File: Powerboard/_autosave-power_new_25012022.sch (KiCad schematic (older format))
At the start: 14 parts

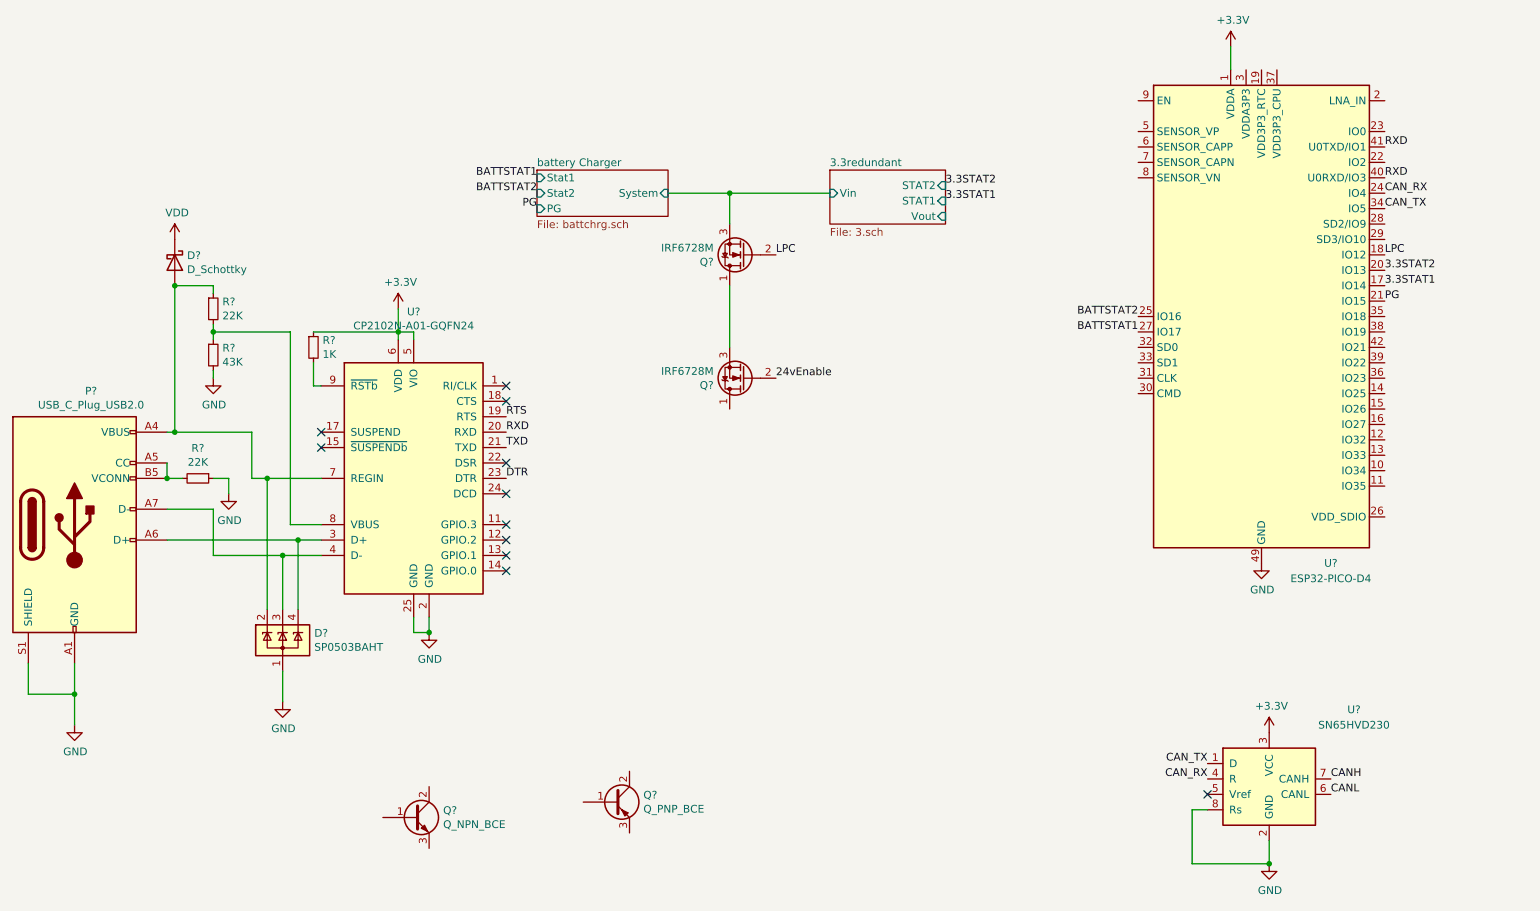
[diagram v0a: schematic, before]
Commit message: 13/02/2022
reverse polarity protection added, some test points, general clear up
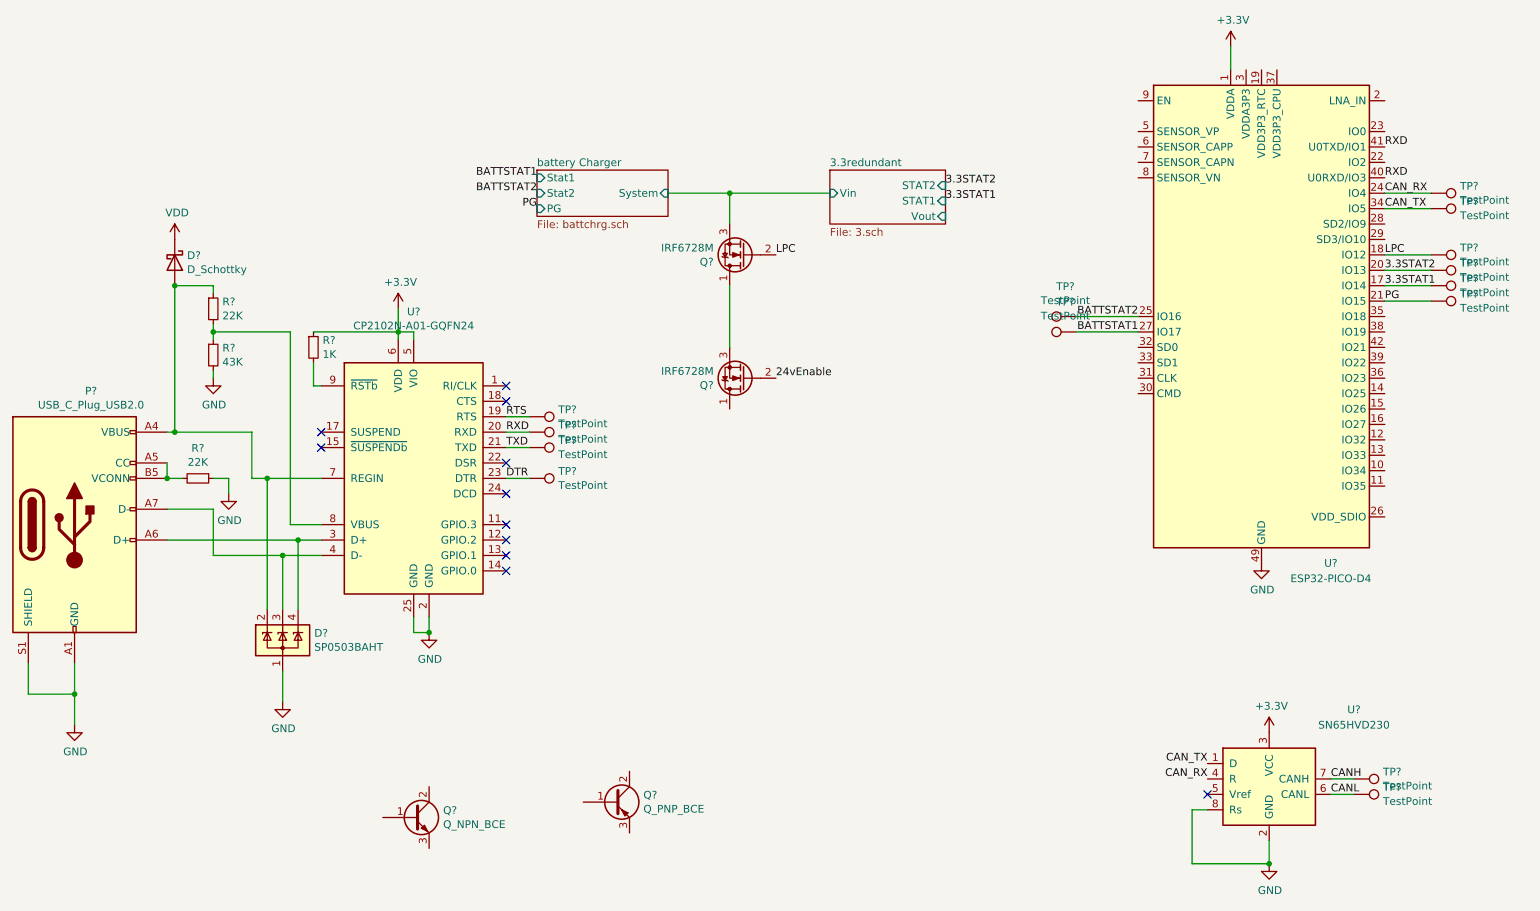
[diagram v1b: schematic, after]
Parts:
- added TP? (x14): TestPoint, symbol Connector:TestPoint
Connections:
- net 3.3STAT1: now also TP?.1
- net 3.3STAT2: now also TP?.1
- net BATTSTAT1: now also TP?.1
- net BATTSTAT2: now also TP?.1
- net CANH: now also TP?.1
- net CANL: now also TP?.1
- net CAN_RX: now also TP?.1
- net CAN_TX: now also TP?.1
- net DTR: now also TP?.1
- net LPC: now also TP?.1
- net PG: now also TP?.1
- net RTS: now also TP?.1
- net RXD: now also TP?.1
- net TXD: now also TP?.1
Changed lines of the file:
@@
 	1    0    0    -1
 $EndComp
+$Comp
+L Connector:TestPoint TP?
+U 1 1 620AFC71
+P 4700 3250
+F 0 "TP?" V 4654 3438 50  0000 L CNN
+F 1 "TestPoint" V 4745 3438 50  0000 L CNN
+F 2 "" H 4900 3250 50  0001 C CNN
+F 3 "~" H 4900 3250 50  0001 C CNN
+	1    4700 3250
+	0    1    1    0
+$EndComp
+$Comp
+L Connector:TestPoint TP?
+U 1 1 620B03B1
+P 4700 3350
+F 0 "TP?" V 4654 3538 50  0000 L CNN
+F 1 "TestPoint" V 4745 3538 50  0000 L CNN
+F 2 "" H 4900 3350 50  0001 C CNN
+F 3 "~" H 4900 3350 50  0001 C CNN
+	1    4700 3350
+	0    1    1    0
+$EndComp
+$Comp
+L Connector:TestPoint TP?
+U 1 1 620B05A4
+P 4700 3450
+F 0 "TP?" V 4654 3638 50  0000 L CNN
+F 1 "TestPoint" V 4745 3638 50  0000 L CNN
+F 2 "" H 4900 3450 50  0001 C CNN
+F 3 "~" H 4900 3450 50  0001 C CNN
+	1    4700 3450
+	0    1    1    0
+$EndComp
+$Comp
+L Connector:TestPoint TP?
+U 1 1 620B0755
+P 4700 3650
+F 0 "TP?" V 4654 3838 50  0000 L CNN
+F 1 "TestPoint" V 4745 3838 50  0000 L CNN
+F 2 "" H 4900 3650 50  0001 C CNN
+F 3 "~" H 4900 3650 50  0001 C CNN
+	1    4700 3650
+	0    1    1    0
+$EndComp
+Wire Wire Line
+	4550 3250 4700 3250
+Wire Wire Line
+	4700 3350 4550 3350
+Wire Wire Line
+	4700 3450 4550 3450
+Wire Wire Line
+	4700 3650 4550 3650
+$Comp
+L Connector:TestPoint TP?
+U 1 1 620B49A6
+P 10550 1800
+F 0 "TP?" V 10504 1988 50  0000 L CNN
+F 1 "TestPoint" V 10595 1988 50  0000 L CNN
+F 2 "" H 10750 1800 50  0001 C CNN
+F 3 "~" H 10750 1800 50  0001 C CNN
+	1    10550 1800
+	0    1    1    0
+$EndComp
+$Comp
+L Connector:TestPoint TP?
+U 1 1 620B4E68
+P 10550 1900
+F 0 "TP?" V 10504 2088 50  0000 L CNN
+F 1 "TestPoint" V 10595 2088 50  0000 L CNN
+F 2 "" H 10750 1900 50  0001 C CNN
+F 3 "~" H 10750 1900 50  0001 C CNN
+	1    10550 1900
+	0    1    1    0
+$EndComp
+Wire Wire Line
+	10550 1800 10250 1800
+Wire Wire Line
+	10550 1900 10250 1900
+$Comp
+L Connector:TestPoint TP?
+U 1 1 620B6EB6
+P 10550 2200
+F 0 "TP?" V 10504 2388 50  0000 L CNN
+F 1 "TestPoint" V 10595 2388 50  0000 L CNN
+F 2 "" H 10750 2200 50  0001 C CNN
+F 3 "~" H 10750 2200 50  0001 C CNN
+	1    10550 2200
+	0    1    1    0
+$EndComp
+$Comp
+L Connector:TestPoint TP?
+U 1 1 620B7211
+P 10550 2300
+F 0 "TP?" V 10504 2488 50  0000 L CNN
+F 1 "TestPoint" V 10595 2488 50  0000 L CNN
+F 2 "" H 10750 2300 50  0001 C CNN
+F 3 "~" H 10750 2300 50  0001 C CNN
+	1    10550 2300
+	0    1    1    0
+$EndComp
+$Comp
+L Connector:TestPoint TP?
+U 1 1 620B73CF
+P 10550 2400
+F 0 "TP?" V 10504 2588 50  0000 L CNN
+F 1 "TestPoint" V 10595 2588 50  0000 L CNN
+F 2 "" H 10750 2400 50  0001 C CNN
+F 3 "~" H 10750 2400 50  0001 C CNN
+	1    10550 2400
+	0    1    1    0
+$EndComp
+$Comp
+L Connector:TestPoint TP?
+U 1 1 620B75EC
+P 10550 2500
+F 0 "TP?" V 10504 2688 50  0000 L CNN
+F 1 "TestPoint" V 10595 2688 50  0000 L CNN
+F 2 "" H 10750 2500 50  0001 C CNN
+F 3 "~" H 10750 2500 50  0001 C CNN
+	1    10550 2500
+	0    1    1    0
+$EndComp
+Wire Wire Line
+	10550 2200 10250 2200
+Wire Wire Line
+	10550 2300 10250 2300
+Wire Wire Line
+	10550 2400 10250 2400
+Wire Wire Line
+	10550 2500 10250 2500
+$Comp
+L Connector:TestPoint TP?
+U 1 1 620BB99A
+P 8250 2600
+F 0 "TP?" V 8445 2672 50  0000 C CNN
+F 1 "TestPoint" V 8354 2672 50  0000 C CNN
+F 2 "" H 8450 2600 50  0001 C CNN
+F 3 "~" H 8450 2600 50  0001 C CNN
+	1    8250 2600
+	0    -1   -1   0
+$EndComp
+$Comp
+L Connector:TestPoint TP?
+U 1 1 620BC227
+P 8250 2700
+F 0 "TP?" V 8445 2772 50  0000 C CNN
+F 1 "TestPoint" V 8354 2772 50  0000 C CNN
+F 2 "" H 8450 2700 50  0001 C CNN
+F 3 "~" H 8450 2700 50  0001 C CNN
+	1    8250 2700
+	0    -1   -1   0
+$EndComp
+Wire Wire Line
+	8650 2700 8250 2700
+Wire Wire Line
+	8650 2600 8250 2600
+$Comp
+L Connector:TestPoint TP?
+U 1 1 620BEC29
+P 10050 5600
+F 0 "TP?" V 10004 5788 50  0000 L CNN
+F 1 "TestPoint" V 10095 5788 50  0000 L CNN
+F 2 "" H 10250 5600 50  0001 C CNN
+F 3 "~" H 10250 5600 50  0001 C CNN
+	1    10050 5600
+	0    1    1    0
+$EndComp
+$Comp
+L Connector:TestPoint TP?
+U 1 1 620BF59B
+P 10050 5700
+F 0 "TP?" V 10004 5888 50  0000 L CNN
+F 1 "TestPoint" V 10095 5888 50  0000 L CNN
+F 2 "" H 10250 5700 50  0001 C CNN
+F 3 "~" H 10250 5700 50  0001 C CNN
+	1    10050 5700
+	0    1    1    0
+$EndComp
+Wire Wire Line
+	10050 5700 9900 5700
+Wire Wire Line
+	10050 5600 9900 5600
 $EndSCHEMATC
